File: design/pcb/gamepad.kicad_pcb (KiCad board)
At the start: 2 copper layers, 66 x 63.5 mm, 21 parts, among them J1 B2B-XH-A, J10 B2B-XH-A, J11 B2B-XH-A, J12 B2B-XH-A, J13 B2B-XH-A, J14 B2B-XH-A, J15 B2B-XH-A, J16 B2B-XH-A, J2 B2B-XH-A, J3 B2B-XH-A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

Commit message: update traces
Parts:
- removed REF** (x4): MountingHole_3mm_Pad, MountingHole:MountingHole_3mm_Pad
- added MH1: MountingHole_3mm_Pad, MountingHole:MountingHole_3mm_Pad, F.Cu at (63.5, 43.2)
- added MH2: MountingHole_3mm_Pad, MountingHole:MountingHole_3mm_Pad, F.Cu at (119.4, 43.2)
- added MH3: MountingHole_3mm_Pad, MountingHole:MountingHole_3mm_Pad, F.Cu at (63.5, 91.4)
- added MH4: MountingHole_3mm_Pad, MountingHole:MountingHole_3mm_Pad, F.Cu at (119.4, 91.4)
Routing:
- net Net-(A1-Pad21): track 37.7 -> 8.69 mm
- net Net-(A1-Pad20): track 43.2 -> 24.2 mm
- net Net-(A1-Pad19): track 54.1 -> 37.0 mm
- net Net-(A1-Pad13): track 34.5 -> 18.5 mm
- net Net-(A1-Pad16): track 48.2 -> 38.4 mm
- net Net-(A1-Pad18): track 52.0 -> 44.5 mm
- net Net-(A1-Pad7): track 31.9 -> 24.8 mm
- net Net-(A1-Pad8): track 16.0 -> 10.8 mm
- net Net-(A1-Pad17): track 44.3 -> 40.8 mm
- net Net-(A1-Pad10): track 26.9 -> 27.5 mm

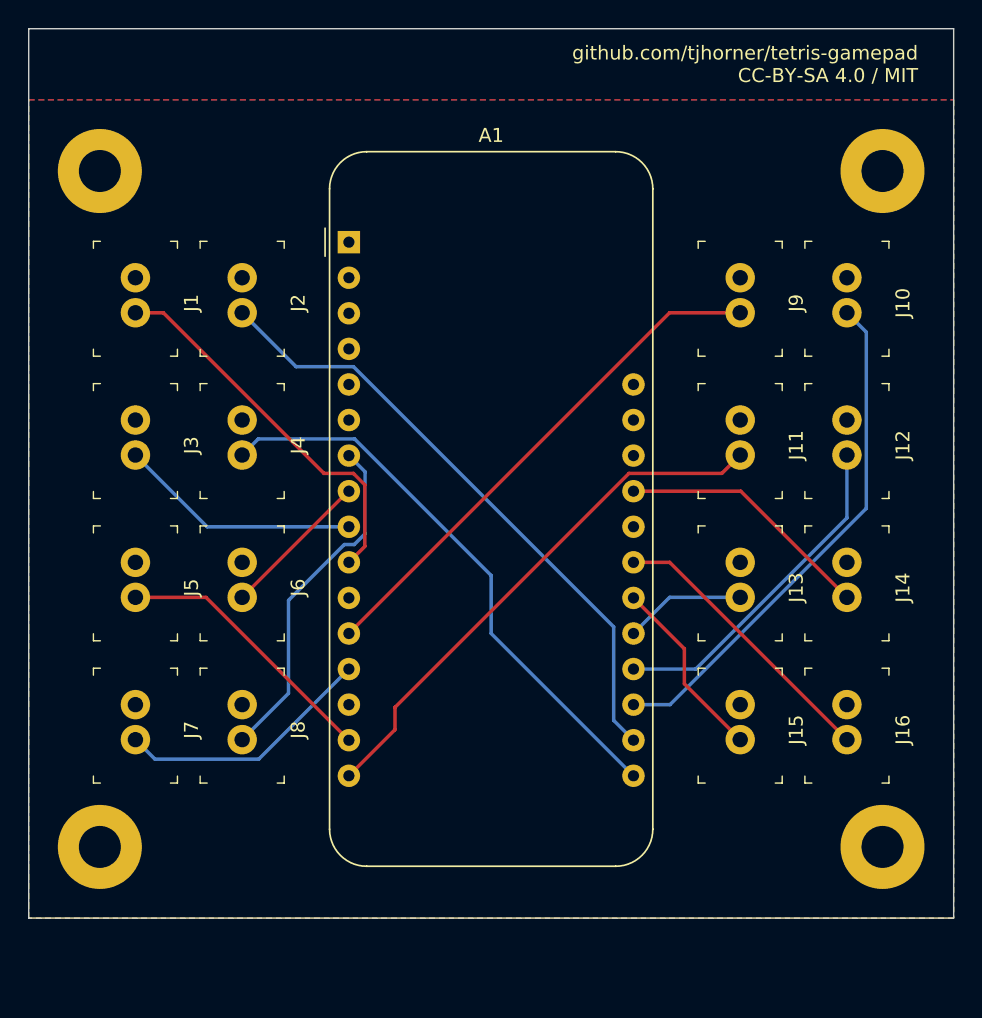
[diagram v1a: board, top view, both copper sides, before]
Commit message: firmware update, fix an oopsie in the pcb
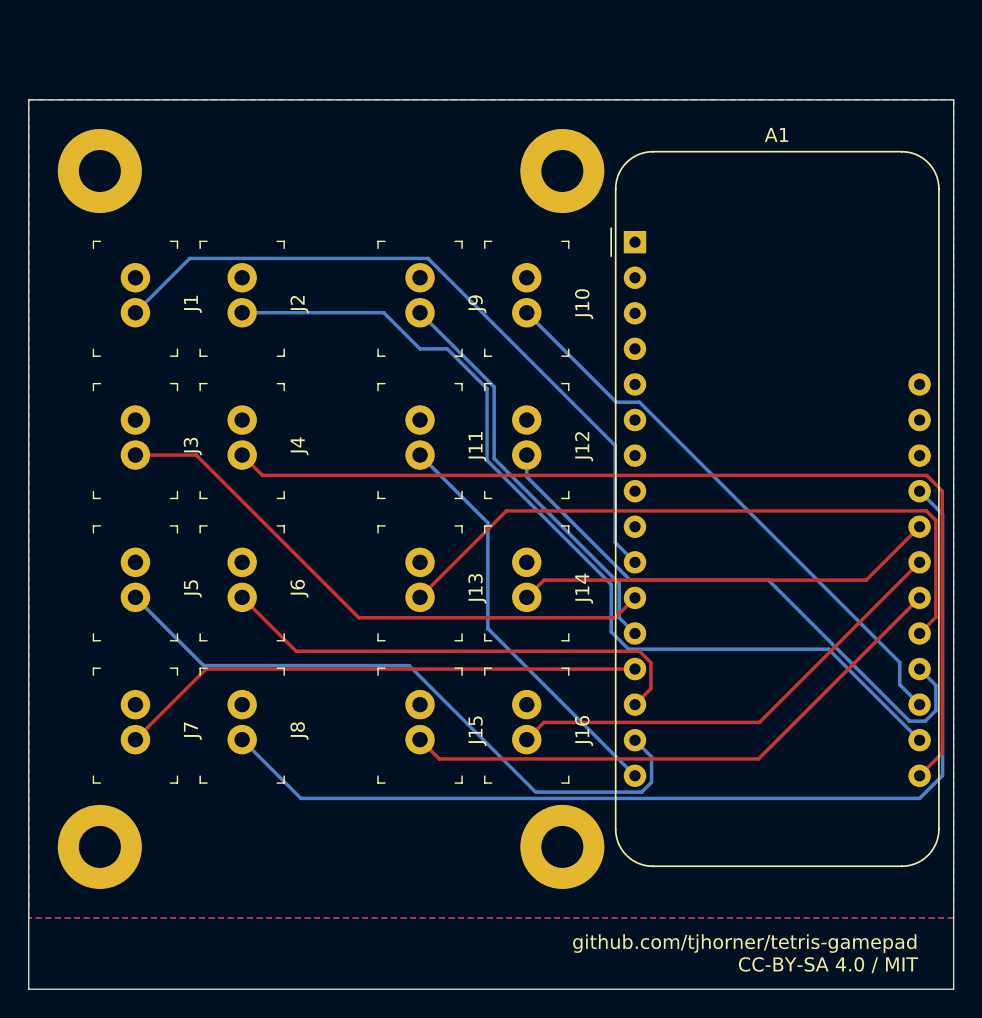
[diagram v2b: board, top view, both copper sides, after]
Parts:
- moved J10 22.9 mm to (94.0, 50.8)
- moved J11 22.9 mm to (86.4, 61.0)
- moved J12 22.9 mm to (94.0, 61.0)
- moved J13 22.9 mm to (86.4, 71.1)
- moved J14 22.9 mm to (94.0, 71.1)
- moved J15 22.9 mm to (86.4, 81.3)
- moved J16 22.9 mm to (94.0, 81.3)
- moved J9 22.9 mm to (86.4, 50.8)
- moved MH2 22.9 mm to (96.5, 43.2)
- moved MH4 22.9 mm to (96.5, 91.4)
- moved A1 20.4 mm to (101.7, 48.3)
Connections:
- A1 pad 11: unconnected-(A1-Pad11) -> Net-(A1-Pad11)
- A1 pad 14: unconnected-(A1-Pad14) -> Net-(A1-Pad14)
- A1 pad 24: unconnected-(A1-Pad24) -> Net-(A1-Pad24)
- A1 pad 7: Net-(A1-Pad7) -> unconnected-(A1-Pad7)
- A1 pad 8: Net-(A1-Pad8) -> unconnected-(A1-Pad8)
- A1 pad 9: Net-(A1-Pad9) -> unconnected-(A1-Pad9)
- J14 pad 2: Net-(A1-Pad25) -> Net-(A1-Pad24)
- J3 pad 2: Net-(A1-Pad9) -> Net-(A1-Pad11)
- J6 pad 2: Net-(A1-Pad8) -> Net-(A1-Pad14)
- J8 pad 2: Net-(A1-Pad7) -> Net-(A1-Pad25)
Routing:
- net Net-(A1-Pad25): track 18.4 -> 73.4 mm
- net Net-(A1-Pad11): track 0.00 -> 41.1 mm
- net Net-(A1-Pad21): track 8.69 -> 48.2 mm
- net Net-(A1-Pad14): track 0.00 -> 34.6 mm
- net Net-(A1-Pad17): track 40.8 -> 72.0 mm
- net Net-(A1-Pad24): track 0.00 -> 30.1 mm
- net Net-(A1-Pad22): track 13.3 -> 41.0 mm
- net Net-(A1-Pad15): track 19.5 -> 46.4 mm
- net Net-(A1-Pad7): track 24.8 -> 0.00 mm
- net Net-(A1-Pad10): track 27.5 -> 50.3 mm
- net Net-(A1-Pad18): track 44.5 -> 66.0 mm
- net Net-(A1-Pad13): track 18.5 -> 37.8 mm
- net Net-(A1-Pad20): track 24.2 -> 41.8 mm
- net Net-(A1-Pad9): track 17.4 -> 0.00 mm
- net Net-(A1-Pad23): track 20.5 -> 33.3 mm
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
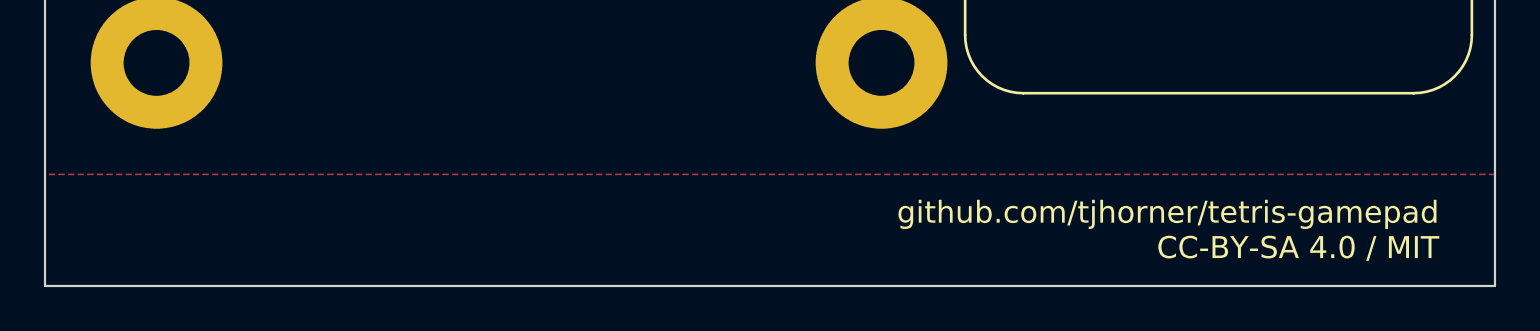
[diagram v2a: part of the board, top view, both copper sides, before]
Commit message: switch away from interrupts, that appears to be faster
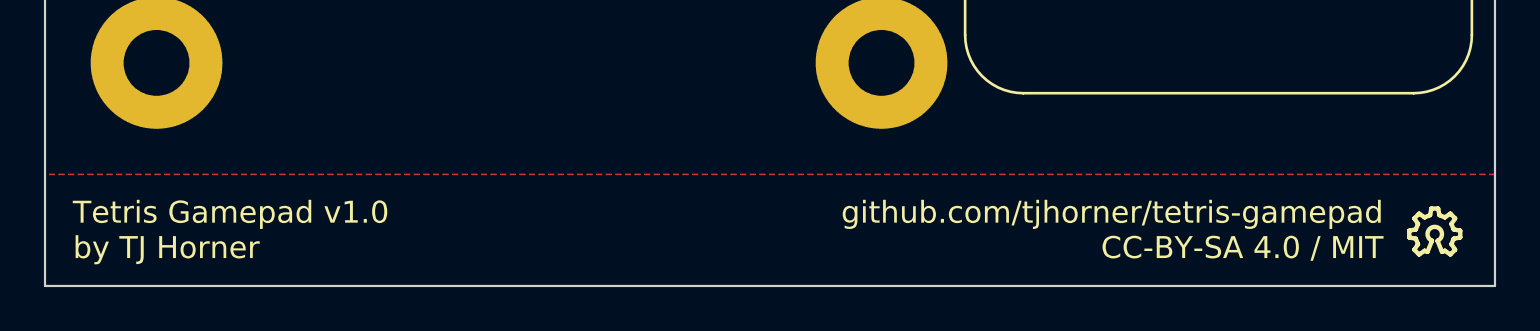
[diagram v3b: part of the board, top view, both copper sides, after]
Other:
- board text added: "Tetris Gamepad v1.0 by TJ Horner"
